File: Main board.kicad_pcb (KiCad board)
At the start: 4 copper layers, 50 x 75 mm, 108 parts, among them CN1 PA001-4P, CN2 PA001-4P, J1 Conn_ARM_SWD_TagConnect_TC203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, J2 Conn_01x03_Pin, J3 Conn_01x03_Pin, J5 Connector, USB-TYPE-C-16P, J6 436500201, J7 Conn_01x04_Pin, J8 Conn_01x04_Pin, Q1 SI7232DN-T1-GE3, Q2 SI7232DN-T1-GE3, SW1 SKRKAEE020, SW2 SKRKAEE020, U1 STM32U575VGTx, U10 TLV75733PDBV, U11 NRVB120VLSFT1G, U12 NRVB120VLSFT1G, U2 TPS62901RPJR, U3 MS5607-02BA03, U7 SN74AHCT125DR, U9 ICM-45686, X1 1XXD32000MBA, Y1 ECS-327TXO-33-TR

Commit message: could be final layout
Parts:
- moved R7 48.7 mm to (150.1, 75.5)
- moved R3 33.9 mm to (180.9, 116.8)
- moved R37 22.0 mm to (172.4, 106.3), turned to -90 degrees
- moved R36 21.8 mm to (170.9, 84.3)
- moved R34 21.7 mm to (173.6, 84.3)
- moved R42 20.6 mm to (189.5, 114.9), turned to 180 degrees
- moved R43 20.4 mm to (184.3, 95.2), turned to -90 degrees
- moved C37 18.6 mm to (153.9, 131.3), turned to 90 degrees
- moved C31 18.1 mm to (171.8, 122.5), turned to -90 degrees
- moved R12 17.6 mm to (180.0, 93.0), turned to 90 degrees
- moved R4 13.4 mm to (174.1, 107.5), turned to 180 degrees
- moved R10 13.0 mm to (166.9, 104.6), turned to 0 degrees
- moved R23 11.4 mm to (175.9, 62.6), turned to 0 degrees
- moved R22 11.1 mm to (164.4, 62.5), turned to -90 degrees
- moved R39 10.8 mm to (160.4, 91.0)
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
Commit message: fix and back to basic
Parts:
- added SW3: SW_SPDT, EasyEDA:SW-TH_3P-L8.8-W3.9-P2.50_SS12D00G3, F.Cu at (52.5, 75.2)
- added SW4: SW_SPDT, EasyEDA:SW-TH_3P-L8.8-W3.9-P2.50_SS12D00G3, F.Cu at (52.5, 80.5)
- C1, C25, C26, C35, C36: footprint PCM_JLCPCB:C_0603 -> PCM_JLCPCB:C_0402
- C28: footprint PCM_JLCPCB:C_0805 -> PCM_JLCPCB:C_0603
- C34: footprint PCM_JLCPCB:C_0805 -> PCM_JLCPCB:C_0402
- CN1, CN2: value PA001-4P -> PA001-6P; footprint EASYEDA:CONN-TH_4P-P5.08_PA001-4P -> Mainboard_local:CONN-TH_6P-P5.00_PA001-6P
- J2: value Conn_01x03_Pin -> Conn_01x02_Pin; footprint Connector_PinHeader_2.54mm:PinHeader_1x03_P2.54mm_Horizontal -> Connector_PinHeader_2.54mm:PinHeader_1x02_P2.54mm_Vertical
- J3: value Conn_01x03_Pin -> Conn_01x02_Pin; footprint Connector_PinHeader_2.54mm:PinHeader_1x03_P2.54mm_Horizontal -> Connector_AMASS:AMASS_XT30PW-F_1x02_P2.50mm_Horizontal
- J7: value Conn_01x04_Pin -> Conn_01x02_Pin; footprint Connector_JST:JST_XH_B4B-XH-A_1x04_P2.50mm_Vertical -> Connector_JST:JST_XH_B2B-XH-A_1x02_P2.50mm_Vertical
- moved C1 142.3 mm to (48.8, 53.1), turned to 0 degrees
- moved R3 139.9 mm to (54.5, 56.8)
- moved CN2 138.5 mm to (63.0, 46.4), turned to 0 degrees
- moved C3 135.4 mm to (48.8, 56.8), turned to 0 degrees
- moved C9 135.1 mm to (48.8, 67.9), turned to 0 degrees
- moved R16 134.5 mm to (57.3, 56.8)
- moved CN1 134.1 mm to (63.0, 36.9), turned to 0 degrees
- moved C10 133.8 mm to (48.8, 69.7), turned to 0 degrees
- moved C8 133.8 mm to (48.8, 66.0)
- moved R13 131.2 mm to (57.3, 53.1)
- moved C15 130.2 mm to (51.6, 58.6)
- moved R4 129.2 mm to (54.5, 58.6), turned to 0 degrees
- moved R11 129.0 mm to (54.5, 69.7), turned to 0 degrees
- moved C36 128.8 mm to (51.6, 71.6), turned to 0 degrees
- moved R1 128.8 mm to (54.5, 53.1), turned to 0 degrees
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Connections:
- CN1 pad 1: Net-(CN1-Pad1) -> PYRO+
- CN1 pad 2: PYRO+ -> Net-(CN1-Pad2)
- CN1 pad 3: Net-(CN1-Pad3) -> Net-(SW3-B)
- CN1 pad 4: PYRO+ -> VBAT-
- CN2 pad 3: PYRO+ -> Net-(SW4-B)
- CN2 pad 4: Net-(CN2-Pad4) -> VBAT-
- H1 pad 1: GNDA -> VBAT-
- H2 pad 1: GNDA -> VBAT-
- H3 pad 1: GNDA -> VBAT-
- H4 pad 1: GNDA -> VBAT-
- J2 pad 1: SERVO1 -> BEC+
- J2 pad 2: +5V -> VBAT-
- J3 pad 1: SERVO2 -> VBAT+
- J3 pad 2: +5V -> VBAT-
- J7 pad 1: +3V3 -> USART1_TX
- J7 pad 2: VBAT- -> USART1_RX
- Q1 pad 5: Net-(CN1-Pad1) -> Net-(CN1-Pad6)
- Q1 pad 6: Net-(CN1-Pad1) -> Net-(CN1-Pad6)
- Q1 pad 7: Net-(CN1-Pad3) -> Net-(CN1-Pad2)
- Q1 pad 8: Net-(CN1-Pad3) -> Net-(CN1-Pad2)
- Q2 pad 5: Net-(CN2-Pad2) -> Net-(CN2-Pad6)
- Q2 pad 6: Net-(CN2-Pad2) -> Net-(CN2-Pad6)
- Q2 pad 7: Net-(CN2-Pad4) -> Net-(CN2-Pad2)
- Q2 pad 8: Net-(CN2-Pad4) -> Net-(CN2-Pad2)
- R40 pad 2: Net-(CN1-Pad3) -> Net-(CN1-Pad2)
- R41 pad 2: Net-(CN1-Pad1) -> Net-(CN1-Pad6)
- R42 pad 2: Net-(CN2-Pad2) -> Net-(CN2-Pad6)
- R43 pad 2: Net-(CN2-Pad4) -> Net-(CN2-Pad2)

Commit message: fix + start leyout
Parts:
- removed C30: 100nF, PCM_JLCPCB:C_0402
- removed D2: MMSZ4683T1G, EASYEDA:SOD-123_L2.8-W1.8-LS3.7-RD
- removed R27: 47kΩ, PCM_JLCPCB:R_0402
- removed R28: 27kΩ, PCM_JLCPCB:R_0402
- moved R5 385.4 mm to (399.8, 231.7)
- moved R8 385.4 mm to (399.8, 235.4)
- moved C15 385.4 mm to (396.9, 229.8)
- moved U7 385.4 mm to (428.9, 208.7)
- moved Card1 324.0 mm to (369.6, 220.6)
- moved R10 324.0 mm to (335.1, 229.8)
- moved R11 324.0 mm to (335.1, 231.6)
- moved R12 324.0 mm to (335.1, 233.5)
- moved R9 324.0 mm to (335.1, 227.9)
- moved R13 317.9 mm to (335.8, 206.3)
- moved R3 317.2 mm to (201.1, 338.0)
- moved R4 317.2 mm to (201.1, 339.8)
- moved J1 317.2 mm to (239.3, 326.1)
- moved R20 317.2 mm to (204.0, 341.7)
- moved SW1 290.0 mm to (171.6, 315.7)
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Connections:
- J2 pad 1: BEC+ -> VBAT-
- J2 pad 2: VBAT- -> BEC+
- J3 pad 1: VBAT+ -> VBAT-
- J3 pad 2: VBAT- -> VBAT+
- J6 pad 1: PYRO+ -> VBAT-
- J6 pad 2: VBAT- -> PYRO+
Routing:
- net PYRO+: track 0.00 -> 42.3 mm
- net BEC+: track 0.00 -> 35.6 mm
- net Net-(SW4-B): track 0.00 -> 7.85 mm
- net +5V: track 0.00 -> 3.15 mm
- added copper zone on F.Cu, net Net-(U10-EN)
- added copper zone on F.Cu, net Net-(U2-SW)
- added copper zone on F.Cu, net PYRO+
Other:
- board size 50 x 75 mm -> 50 x 85 mm

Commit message: update
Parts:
- moved SW3 10.8 mm to (132.9, 125.9)
- moved SW4 9.17 mm to (132.9, 91.4)
- moved C35 3.32 mm to (151.9, 59.4), turned to 90 degrees
- moved Q2 2.40 mm to (133.0, 74.0)
- moved R37 2.40 mm to (132.6, 77.7)
- moved R38 2.40 mm to (133.8, 77.7)
- moved R42 2.40 mm to (134.1, 69.9)
- moved R43 2.40 mm to (132.1, 69.9)
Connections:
- CN1 pad 3: Net-(SW3-B) -> Net-(CN1-Pad3)
- CN1 pad 6: Net-(CN1-Pad6) -> Net-(SW3-B)
- CN2 pad 3: Net-(SW4-B) -> Net-(CN2-Pad3)
- CN2 pad 6: Net-(CN2-Pad6) -> Net-(SW4-B)
- Q1 pad 5: Net-(CN1-Pad6) -> Net-(CN1-Pad3)
- Q1 pad 6: Net-(CN1-Pad6) -> Net-(CN1-Pad3)
- Q2 pad 5: Net-(CN2-Pad6) -> Net-(CN2-Pad3)
- Q2 pad 6: Net-(CN2-Pad6) -> Net-(CN2-Pad3)
- R41 pad 2: Net-(CN1-Pad6) -> Net-(CN1-Pad3)
- R42 pad 2: Net-(CN2-Pad6) -> Net-(CN2-Pad3)
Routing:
- net BEC+: track 35.6 -> 0.00 mm
- net PYRO+: track 42.3 -> 24.0 mm
- net Net-(SW4-B): track 7.85 -> 0.00 mm
- net Net-(CN2-Pad2): track 0.00 -> 4.20 mm
- net Net-(CN1-Pad2): track 0.00 -> 4.15 mm
- added copper zone on F.Cu, net Net-(CN1-Pad2)
- added copper zone on F.Cu, net Net-(CN1-Pad3)
- added copper zone on F.Cu, net Net-(CN2-Pad2)
- added copper zone on F.Cu, net Net-(CN2-Pad3)

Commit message: koiiin
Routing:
- net Net-(CN2-Pad3): track 0.00 -> 1.60 mm
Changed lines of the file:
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@@
+	)
+	(segment
+		(start 129.1205 77.976)
+		(end 127.5175 77.976)
+		(width 2.5)
+		(layer "In2.Cu")
+		(net 25)
 	)
 	(segment

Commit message: 80%layout
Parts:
- J3: moved to B.Cu
- moved R8 306.6 mm to (132.2, 85.9)
- moved U7 300.4 mm to (142.3, 118.8), turned to 180 degrees
- moved R5 289.8 mm to (132.2, 120.4)
- moved C15 272.1 mm to (146.0, 124.6), turned to -90 degrees
- moved Card1 257.4 mm to (161.2, 69.7), turned to 90 degrees
- moved J5 237.2 mm to (151.2, 55.8), turned to 180 degrees
- moved C37 231.7 mm to (152.9, 68.7), turned to 180 degrees
- moved R12 228.2 mm to (157.7, 90.0), turned to 45 degrees
- moved R11 225.9 mm to (158.5, 90.8), turned to 45 degrees
- moved R23 220.1 mm to (148.7, 60.1), turned to 180 degrees
- moved R22 218.8 mm to (153.2, 60.1)
- moved R10 216.2 mm to (156.0, 108.7), turned to -45 degrees
- moved R9 215.5 mm to (155.2, 109.4), turned to -45 degrees
- moved D1 214.3 mm to (150.9, 63.4), turned to 180 degrees
- moved R13 210.4 mm to (159.4, 91.5), turned to 45 degrees
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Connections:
- U1 pad 7: FIRE_D -> FIRE_C
- U1 pad 9: FIRE_C -> FIRE_D
- U7 pad 2: PWM1 -> PWM2
- U7 pad 5: PWM2 -> PWM1
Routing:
- net BEC+: track 0.00 -> 55.2 mm
- net FIRE_B: track 0.00 -> 13.2 mm
- net +5V: track 3.15 -> 0.00 mm
- net Net-(CN2-Pad3): track 1.60 -> 0.00 mm
- removed copper zone on F.Cu, net Net-(U2-SW)

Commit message: CHECKPOINT
the longggggggggggg wayyyyyyy 50x85 mm
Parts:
- moved R7 255.1 mm to (154.9, 81.0), turned to 90 degrees
- moved D7 250.6 mm to (210.3, 108.2)
- moved D6 250.6 mm to (210.3, 106.3)
- moved D5 250.4 mm to (210.9, 104.8)
- moved R21 244.9 mm to (213.5, 101.6)
- moved R29 244.6 mm to (213.4, 108.6)
- moved R3 244.6 mm to (163.1, 96.4), turned to 135 degrees
- moved R39 244.0 mm to (213.7, 104.6)
- moved R44 243.4 mm to (214.2, 106.7)
- moved R20 242.3 mm to (169.3, 101.9), turned to -90 degrees
- moved D4 242.0 mm to (210.1, 101.9)
- moved R4 240.2 mm to (161.9, 102.9), turned to 135 degrees
- moved J1 237.4 mm to (166.6, 100.1), turned to 90 degrees
- moved C2 236.4 mm to (170.0, 96.3), turned to -90 degrees
- moved SW2 235.8 mm to (157.5, 83.4), turned to 90 degrees
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
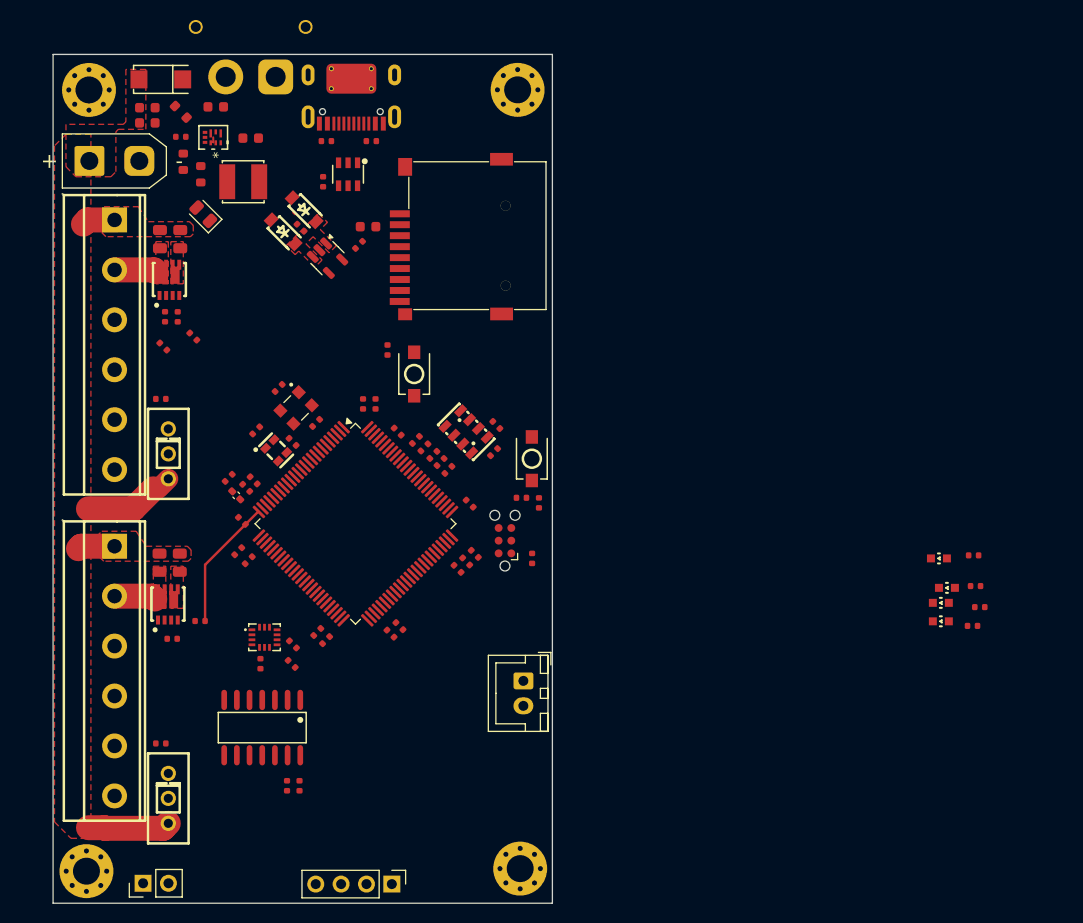
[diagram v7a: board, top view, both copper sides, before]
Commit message: add LED for Barometer and IMU
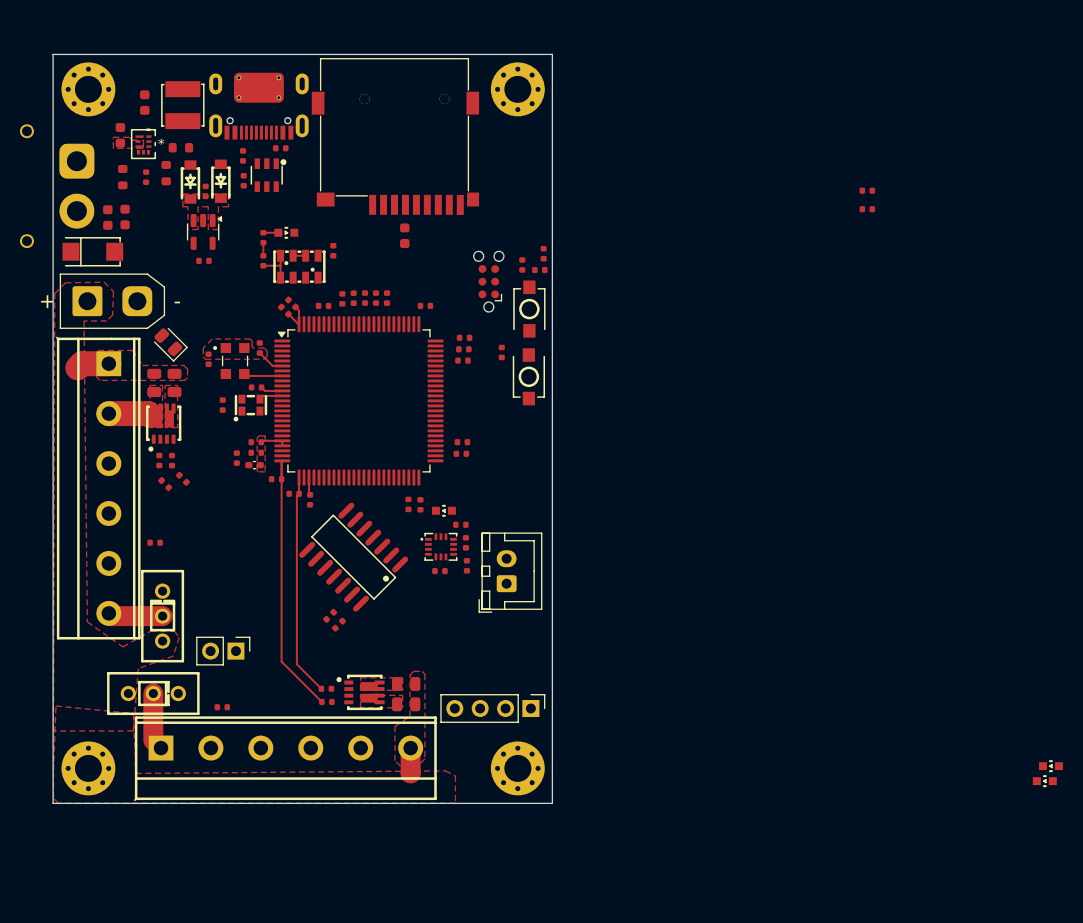
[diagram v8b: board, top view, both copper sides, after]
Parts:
- removed R29, R39, R44: 470Ω, PCM_JLCPCB:R_0402
- added R17: 2kΩ, PCM_JLCPCB:R_0402, F.Cu at (142.4, 69.8)
- added R18: 2kΩ, PCM_JLCPCB:R_0402, F.Cu at (162.2, 98.5)
- added R6: 2kΩ, PCM_JLCPCB:R_0402, F.Cu at (202.9, 65.0)
- R14: value 47kΩ -> 2kΩ
- R21: value 470Ω -> 47kΩ
- moved R21 77.0 mm to (142.4, 72.1), turned to -90 degrees
- moved D4 73.0 mm to (144.7, 69.3), turned to 180 degrees
- moved D7 51.0 mm to (160.5, 97.1)
- moved R14 44.6 mm to (202.9, 66.9), turned to 0 degrees
- moved R20 30.5 mm to (170.5, 71.4), turned to 90 degrees
- moved R40 27.5 mm to (156.7, 114.4), turned to 180 degrees
- moved R41 26.7 mm to (156.7, 116.5), turned to 180 degrees
- moved J1 26.0 mm to (165.0, 74.2)
- moved J2 25.0 mm to (139.7, 111.2), turned to -90 degrees
- moved C18 23.9 mm to (149.4, 71.1), turned to 90 degrees
- moved C2 23.9 mm to (168.3, 72.5), turned to 90 degrees
- moved U3 23.5 mm to (146.0, 72.7), turned to -90 degrees
- moved R1 22.9 mm to (170.1, 73.0), turned to 180 degrees
- moved J8 22.4 mm to (169.2, 116.9)
- moved C9 21.7 mm to (162.6, 79.8), turned to 0 degrees
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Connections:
- CN1 pad 1: PYRO+ -> Net-(SW3-B)
- CN1 pad 2: Net-(CN1-Pad2) -> SERVO1
- CN1 pad 3: Net-(CN1-Pad3) -> VBAT-
- CN1 pad 4: VBAT- -> Net-(CN1-Pad4)
- CN1 pad 5: SERVO1 -> Net-(CN1-Pad5)
- CN1 pad 6: Net-(SW3-B) -> PYRO+
- Q1 pad 5: Net-(CN1-Pad3) -> Net-(CN1-Pad5)
- Q1 pad 6: Net-(CN1-Pad3) -> Net-(CN1-Pad5)
- Q1 pad 7: Net-(CN1-Pad2) -> Net-(CN1-Pad4)
- Q1 pad 8: Net-(CN1-Pad2) -> Net-(CN1-Pad4)
- R14 pad 1: +3V3 -> Net-(D6-A)
- R14 pad 2: MS5607_CS -> PB6
- R21 pad 1: Net-(D4-A) -> +3V3
- R21 pad 2: +3V3 -> MS5607_CS
- R40 pad 2: Net-(CN1-Pad2) -> Net-(CN1-Pad4)
- R41 pad 2: Net-(CN1-Pad3) -> Net-(CN1-Pad5)
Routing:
- net BEC+: track 55.2 -> 14.2 mm
- net FIRE_A: track 0.00 -> 22.3 mm
- net PYRO+: track 24.0 -> 5.84 mm
- net FIRE_B: track 13.2 -> 25.9 mm
- net +3V3: track 0.00 -> 11.4 mm
- net Net-(SW4-B): track 0.00 -> 5.50 mm
- net Net-(SW3-B): track 0.00 -> 4.69 mm
- net Net-(CN1-Pad2): track 4.15 -> 0.00 mm
- net MS5607_CS: track 0.00 -> 3.92 mm
- net LSE_IN: track 0.00 -> 3.89 mm
- net +3.3VA: track 0.00 -> 2.66 mm
- net HSE_IN: track 0.00 -> 2.37 mm
- net Net-(D4-A): track 0.00 -> 1.50 mm
- net VBAT-: track 0.00 -> 1.25 mm
- added copper zone on F.Cu, net +3.3VA
- added copper zone on F.Cu, net +3V3
- added copper zone on F.Cu, net Net-(CN1-Pad4)
- added copper zone on F.Cu, net Net-(CN1-Pad5)
- added copper zone on F.Cu, net VBAT+
- removed copper zone on F.Cu, net Net-(CN1-Pad2)
- removed copper zone on F.Cu, net Net-(CN1-Pad3)
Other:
- board size 50 x 85 mm -> 50 x 75 mm
